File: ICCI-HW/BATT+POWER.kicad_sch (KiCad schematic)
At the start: 21 parts

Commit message: updated
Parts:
- removed D?: 3V3_LED, LED_SMD:LED_0603_1608Metric, symbol Device:LED
- removed J?: BATT IN, Connector_Molex:Molex_Micro-Fit_3.0_43650-0200_1x02_P3.00mm_Horizontal, symbol Connector_Generic:Conn_01x02
- removed R?: 510, Resistor_SMD:R_0603_1608Metric, symbol Device:R
- added BT? (x2): Li-Ion 18650, symbol Device:Battery_Cell
- added C? (x3): 10u, symbol Device:C
- added C?: 47u, symbol Device:C
- added D?: 1V8_LED, LED_SMD:LED_0603_1608Metric, symbol Device:LED
- added D?: 3V3_LED, LED_SMD:LED_0603_1608Metric, symbol Device:LED
- added D?: D_Schottky, symbol Device:D_Schottky
- added D?: TVS XXXXX, Diode_SMD:D_SMA, symbol Diode:1.5KExxA
- added JP?: SolderJumper_2_Open, symbol Jumper:SolderJumper_2_Open
- added Q? (x3): SSM3K15AMFV,L3F, symbol Device:Q_NMOS_GSD
- added R? (x3): R, symbol Device:R
- added R?: 680R, Resistor_SMD:R_0603_1608Metric, symbol Device:R
- added R?: 180R, Resistor_SMD:R_0603_1608Metric, symbol Device:R
- added U?: MAX77962EWJ12+, symbol ICCI-LIB:MAX77962EWJ12+
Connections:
- net +1V8: now also D?.2 (A)
- net +3V3: now also D?.2 (A), JP?.2 (B); no longer C?.1, C?.1, L?.2
- net GND: now also BT?.2 (-), C?.2, C?.2, C?.2, C?.2, D?.2 (A2), Q?.3 (D), Q?.3 (D), Q?.3 (D), R?.2, R?.2, U?.C5 (GND_1), U?.C6 (GND_2), U?.C7 (GND_3), U?.D1 (PGND_1), U?.D2 (PGND_2), U?.D3 (PGND_3), U?.D4 (PGND_4), U?.D6 (GND_4)
- net BATT_IN renamed SYS
- net SYS: now also C?.1, D?.1 (K), U?.E4 (SYS_1), U?.F1 (SYS_2), U?.F2 (SYS_3), U?.F3 (SYS_4), U?.F4 (SYS_5)
- net VCC renamed SW_VIN
- new net: C?.1, C?.1, JP?.1 (A), L?.2
- new net: Q?.2 (S), R?.2 (x2)
- new net: D?.1 (K), R?.1 (x2)
- new net: Q?.2 (S), R?.1
- new net: BT?.1 (+), BT?.2 (-)
- new net AVL: U?.A5 (AVL)
- new net BATT: BT?.1 (+), C?.1, D?.2 (A), U?.E5 (BATT_1), U?.F5 (BATT_2), U?.G5 (BATT_3)
- new net CHR0: Q?.1 (G)
- new net CHR1: Q?.1 (G)
- new net CHREN: Q?.1 (G)
- new net ISET: R?.1, R?.1, R?.2
- new net VBUS: C?.1, C?.1, D?.1 (A1), U?.B1 (CHGIN_1), U?.B2 (CHGIN_2), U?.B3 (CHGIN_3), U?.B4 (CHGIN_4)
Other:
- note added: "Analog GND"
- note added: "Buck test"
- note added: "Power GND"
- note added: "V_{OUT}=0.768(1+R_{1}/R_{2})"
- note removed: "L1 : Montare dopo aver testato che switching funziona"
- note removed: "V_{OUT}=0.768(1+R_{1}/R_{2}) For a V_{OUT}=3.3V the ratio should be 3.296875"
- moved on the sheet: C?, D?, F?, L?, R?, U?

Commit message: updated
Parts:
- removed JP?: SolderJumper_2_Open, symbol Jumper:SolderJumper_2_Open
- added R?: 0R, symbol Device:R
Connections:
- net +3V3: now also R?.2
- net at C?.1, C?.1, L?.2: now also R?.1
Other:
- moved on the sheet: BT?, C?, D?, F?, L?, Q?, R?, U?

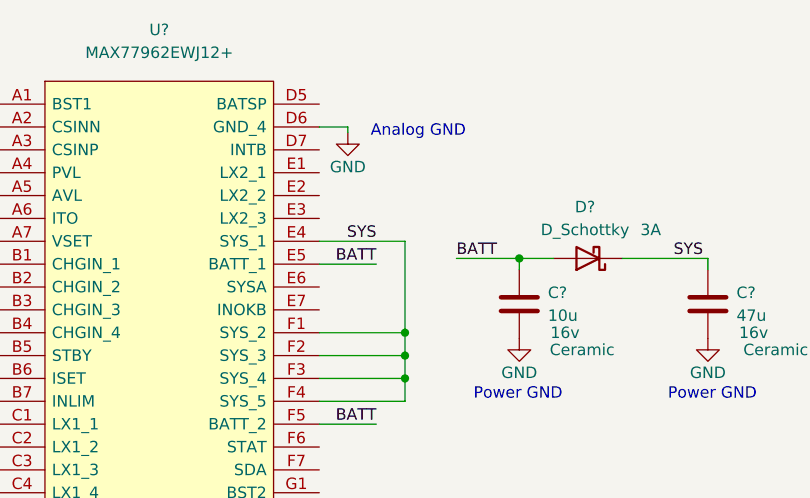
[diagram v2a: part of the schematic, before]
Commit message: add GPIO Expansion
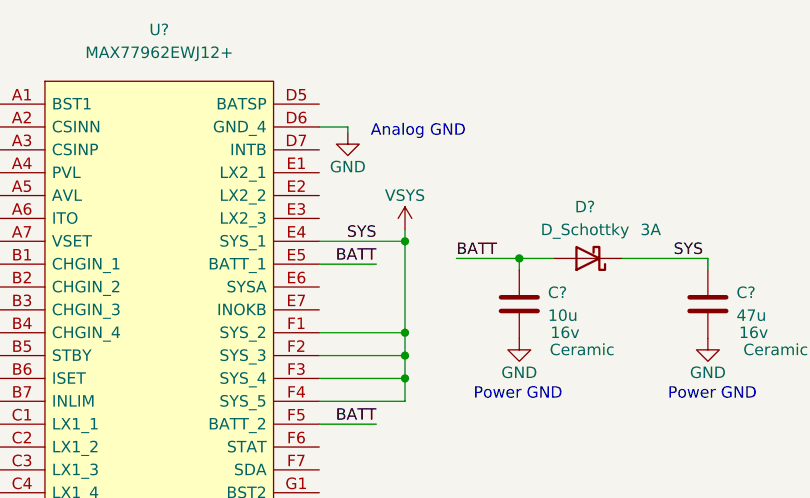
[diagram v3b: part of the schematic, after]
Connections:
- net SYS renamed VCC
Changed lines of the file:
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@@
   (junction (at 153.67 133.35) (diameter 0) (color 0 0 0 0)
   )
+  (junction (at 160.655 42.545) (diameter 0) (color 0 0 0 0)
+  )
   (junction (at 114.3 75.565) (diameter 0) (color 0 0 0 0)
   )
@@
   )
   (wire (pts (xy 160.655 52.705) (xy 160.655 55.245))
+    (stroke (width 0) (type default) (color 0 0 0 0))
+  )
+  (wire (pts (xy 160.655 41.275) (xy 160.655 42.545))
     (stroke (width 0) (type default) (color 0 0 0 0))
   )
@@
     (pin "2")
   )
+  (symbol (lib_id "power:VSYS") (at 160.655 41.275 0) (unit 1)
+    (in_bom yes) (on_board yes)
+    (property "Reference" "#PWR?" (id 0) (at 160.655 45.085 0)
+      (effects (font (size 1.27 1.27)) hide)
+    )
+    (property "Value" "VSYS" (id 1) (at 160.655 37.465 0))
+    (property "Footprint" "" (id 2) (at 160.655 41.275 0)
+      (effects (font (size 1.27 1.27)) hide)
+    )
+    (property "Datasheet" "" (id 3) (at 160.655 41.275 0)
+      (effects (font (size 1.27 1.27)) hide)
+    )
+    (pin "1")
+  )
   (symbol (lib_id "power:GND") (at 31.115 64.135 0) (unit 1)

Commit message: updated
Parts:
- removed C? (x3): 10u, symbol Device:C
- removed C?: 47u, symbol Device:C
- removed D?: TVS XXXXX, Diode_SMD:D_SMA, symbol Diode:1.5KExxA
- removed Q? (x3): SSM3K15AMFV,L3F, symbol Device:Q_NMOS_GSD
- removed R? (x3): R, symbol Device:R
- removed U?: MAX77962EWJ12+, symbol ICCI-LIB:MAX77962EWJ12+
- added C? (x2): 0.22u, symbol Device:C
- added C? (x3): 10u, symbol Device:C
- added C? (x2): 15n, symbol Device:C
- added C? (x2): 47u, symbol Device:C
- added C? (x2): 4.7u, symbol Device:C
- added C?: 100n, symbol Device:C
- added C?: 1u, Capacitor_SMD:C_0603_1608Metric, symbol Device:C
- added D?: 3V3_LED, LED_SMD:LED_0603_1608Metric, symbol Device:LED
- added JP? (x4): SolderJumper_3_Bridged12, symbol Jumper:SolderJumper_3_Bridged12
- added L?: 1.5u, symbol Device:L
- added NT?: NetTie_2, symbol Device:NetTie_2
- added R?: 680R, Resistor_SMD:R_0603_1608Metric, symbol Device:R
- added R?: 10m 1206 (?), symbol Device:R
- added R? (x2): 10k, symbol Device:R
- added R? (x2): 10R, symbol Device:R
- added R?: 4.7R, symbol Device:R
- added R?: 39,2k, symbol Device:R
- added R? (x2): 200k, symbol Device:R
- added R?: 140k, symbol Device:R
- added R?: 69,8k, symbol Device:R
- added R?: DNP, symbol Device:R
- added R?: 100k, symbol Device:R
- added RN?: 10k, Resistor_THT:R_Array_SIP4, symbol Device:R_Network03
- added TH?: NTC, symbol Device:Thermistor_NTC
- added U?: MAX77962EWJ12+, symbol ICCI-LIB:MAX77962EWJ12+
- D? (x2): Color Red -> Green
- D?: value SMA S1B -> RB160QS-40T18R
- F?: value 2016L050MR -> MF-LSMF075X
- R?: value 0R -> 0R BUCK TEST
- U?: value NCV8164ASN180T1G_ -> NCV8164ASN180T1G
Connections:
- net +3V3: now also D?.2 (A), R?.1
- net 1V8_EN: now also R?.2
- net AVL: now also C?.1, R?.1, R?.2, U?.A5 (AVL)
- net GND: now also C?.1, C?.1, C?.2, C?.2, C?.2, C?.2, C?.2, C?.2, C?.2, C?.2, R?.2, R?.2, R?.2, R?.2, RN?.1 (common), TH?.2, U?.C5 (GND_1), U?.C6 (GND_2), U?.C7 (GND_3), U?.D1 (PGND_1), U?.D2 (PGND_2), U?.D3 (PGND_3), U?.D4 (PGND_4), U?.D6 (GND_4), U?.G4 (BATSN)
- net ISET: now also JP?.2 (C), U?.B6 (ISET)
- net SCL1: now also U?.G7 (SCL)
- net SDA1: now also U?.F7 (SDA)
- net VBUS: now also R?.1, R?.1
- net VCC: now also C?.1, C?.1, U?.E4 (SYS_1), U?.F1 (SYS_2), U?.F2 (SYS_3), U?.F3 (SYS_4), U?.F4 (SYS_5)
- net 1V8_PG: no longer names the net of R?.2, U?.4 (PG)
- net BATT renamed +BATT
- net +BATT: now also C?.1, NT?.2, U?.E5 (BATT_1), U?.F5 (BATT_2), U?.G5 (BATT_3)
- new net: D?.1 (K), R?.1
- new net: C?.1, U?.G1 (BST2)
- new net: C?.2, L?.2, U?.E1 (LX2_1), U?.E2 (LX2_2), U?.E3 (LX2_3)
- new net: C?.1, U?.A1 (BST1)
- new net: C?.2, L?.1, U?.C1 (LX1_1), U?.C2 (LX1_2), U?.C3 (LX1_3), U?.C4 (LX1_4)
- new net BATSP: NT?.1, U?.D5 (BATSP)
- new net CHGIN: C?.1, C?.1, R?.1, R?.2, U?.B1 (CHGIN_1), U?.B2 (CHGIN_2), U?.B3 (CHGIN_3), U?.B4 (CHGIN_4)
- new net CSINN: C?.2, C?.2, R?.2, U?.A2 (CSINN)
- new net CSINP: C?.1, C?.2, R?.2, U?.A3 (CSINP)
- new net DISQBAT: RN?.3 (R2), U?.G2 (DISQBAT)
- new net INLIM: JP?.2 (C), U?.B7 (INLIM)
- new net INLIM_R: JP?.1 (A), R?.1
- new net ISET_R: JP?.3 (B), R?.1
- new net ITO: JP?.2 (C), U?.A6 (ITO)
- new net ITO_R: JP?.1 (A), R?.1
- new net MAX_INOKB: R?.2, U?.E7 (INOKB)
- new net MAX_INTB: R?.2, U?.D7 (INTB)
- new net OTGEN: RN?.2 (R1), U?.G3 (OTGEN)
- new net PVL: C?.1, JP?.1 (A), JP?.3 (B), JP?.3 (B), JP?.3 (B), R?.1, R?.1, R?.1, R?.1, U?.A4 (PVL)
- new net STAT: R?.2, U?.F6 (STAT)
- new net STBY: RN?.4 (R3), U?.B5 (STBY)
- new net SYSA: C?.1, U?.E6 (SYSA)
- new net THM: R?.2, TH?.1, U?.G6 (THM)
- new net VSET: JP?.2 (C), U?.A7 (VSET)
- new net VSET_R: JP?.1 (A), R?.1
- new net ~{BATT_S_LED}: R?.2
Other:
- note added: "0.75A Hold 1.5A Trip"
- note added: "1.5A"
- note added: "2A CHGIN"
- note added: "2S1P 18650 Li-Ion."
- note added: "3V3 Peripherals MAX absolute ratings: - ESP32 = 500mA (min required by DS) - GPIO Expander = 300mA (with all pin max output) - CP2102N = 50mA - 4 Sensors = 10mA - GPS/RTC = 70mA/50mA - Buzzer = 35mA -------------------------- TOT < 1.5A -> Real probably < 0.7A"
- note added: "75mA top-off"
- note added: "8.4V"
- note added: "==>"
- note added: "ATT!"
- note added: "As close as possible to battery terminals."
- note added: "Batt. Insertion Protection"
- note added: "Battery"
- note added: "Battery Management"
- note added: "Battery Status LED"
- note added: "Check if USB is max 1.5A. Sembrerebbe di no da USB BC 1.2"
- note added: "If at least one has no valid resistor value (ISET) charging is disabled by default and need to be set by I2C (choosen for safety reasons)."
- note added: "If batteries The regulator always priorities the system, the remaining power will be delivered to battery if charging. So, if charging at 1.5A and system is using 1A, battery charger will get only 0.5A. If Input power is not enough to power the system, battery will output current to system. So, if available input power is 0.5A and system is using 1A, if battery are charged they will deliver the r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"
- note added: "Led off batt normal, Led on batt charging, Led blinking slow batt low (in order to save energy)."
- note added: "Max 1.5A"
- note added: "NON DISPONIBILE"
- note added: "Tcold = 4.1 °C Thot = 53.2 °C"
- note added: "Temp Protection"
- note added: "WARNING, NO REVERSE POLARITY PROTECTION!"
- note removed: "1A"
- note removed: "2S1P 18650 Li-Ion"
- note removed: "Buck test"
- note removed: "Max XXA"
- note removed: "XXA Hold XXA Trip"
- moved on the sheet: BT?, C?, D?, F?, L?, R?, U?

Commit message: schematic V1.0
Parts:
- removed C?: 100n, Capacitor_SMD:C_0603_1608Metric, symbol Device:C
- removed C?: 10u, Capacitor_SMD:C_0805_2012Metric, symbol Device:C
- removed D?: 1V8_LED, LED_SMD:LED_0603_1608Metric, symbol Device:LED
- removed R?: 10k, Resistor_SMD:R_0603_1608Metric, symbol Device:R
- removed R?: 180R, Resistor_SMD:R_0603_1608Metric, symbol Device:R
- removed U?: TPS563201, Package_TO_SOT_SMD:SOT-23-6, symbol Regulator_Switching:TPS563200
- added U602: AP62301WU-7, symbol ICCI-LIB:AP62301WU-7
- C602: renamed from C?; Tech (none) -> Cer. low ESR; Voltage 16V -> 25V
- D603: renamed from D?; value RB160QS-40T18R -> PMEG3020EJ,115
- D605: renamed from D?; Color Green -> Red
- D606: renamed from D?; value D_Schottky -> VSSAF3L45HM3_A/I
- L601: renamed from L?; value 2.2u -> 3.3u
- R602, R615: renamed from R?; value 680R -> 510R
- R606: renamed from R?; value 33k -> 31,6k
- R607: renamed from R?; Tolerance (none) -> 1%
- R608: renamed from R?; value 10m 1206 (?) -> 10m; footprint (none) -> Resistor_SMD:R_1206_3216Metric; Package (none) -> 1206
- R619: renamed from R?; value 39,2k -> 22,6k
- gave numbers to parts that had none: 46
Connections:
- net +3V3: no longer R606.1
- net GND: now also U602.3 (GND)
- net SW_BST: now also U602.4 (BST)
- net SW_FB: now also U602.6 (FB)
- net SW_NODE: now also U602.2 (SW)
- net SW_VIN: now also U602.1 (VIN)
- net SW_NODE_OUT: now reaches C610.1, C612.1, L601.2, R614.1
- net SW_NODE_OUT: now also R606.1
- no-connect marks 0 -> 1
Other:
- note added: "2.5A Input max"
- note added: "2A"
- note added: "Check if USB BC is max 1.5A. From USB BC 1.2 Specs seems that I>1.5A are allowed."
- note added: "Floating for automatic startup"
- note added: "Low ESR"
- note removed: "1.5A"
- note removed: "2A CHGIN"
- note removed: "Check if USB is max 1.5A. Sembrerebbe di no da USB BC 1.2"
- note removed: "NON DISPONIBILE"
- note removed: "V_{OUT}=0.768(1+R_{1}/R_{2})"
- moved on the sheet: C602, C608, C610, C612, D602, D603, D605, F601, L601, R606, R607, R614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

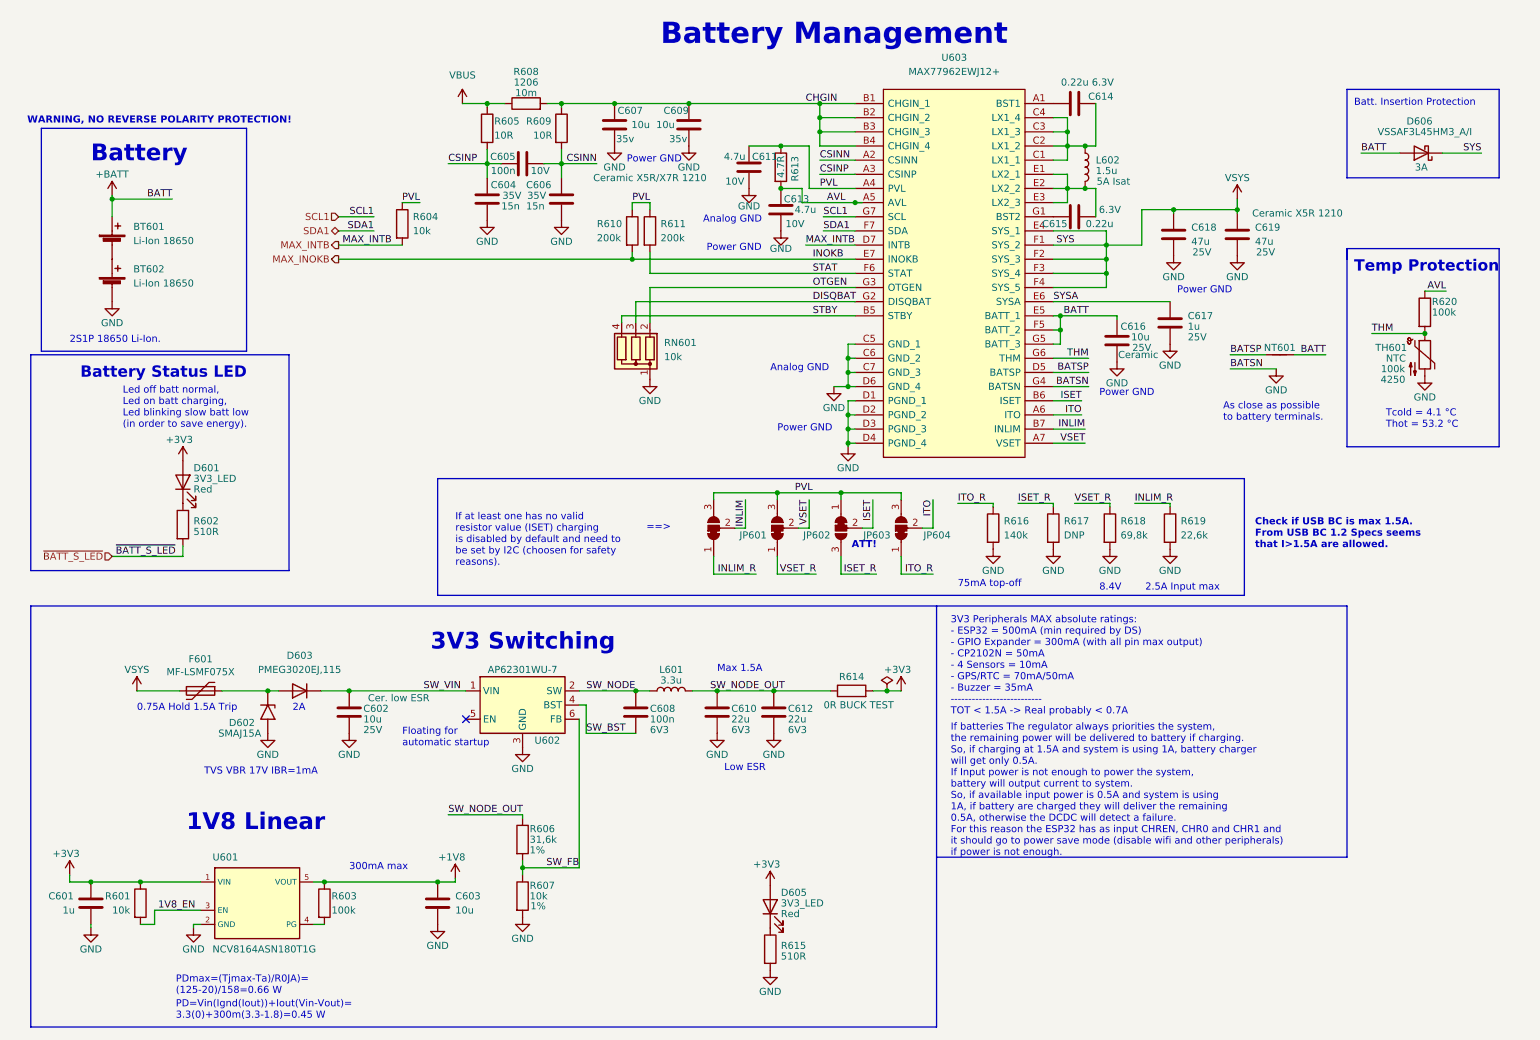
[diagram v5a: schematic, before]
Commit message: footprint assigned
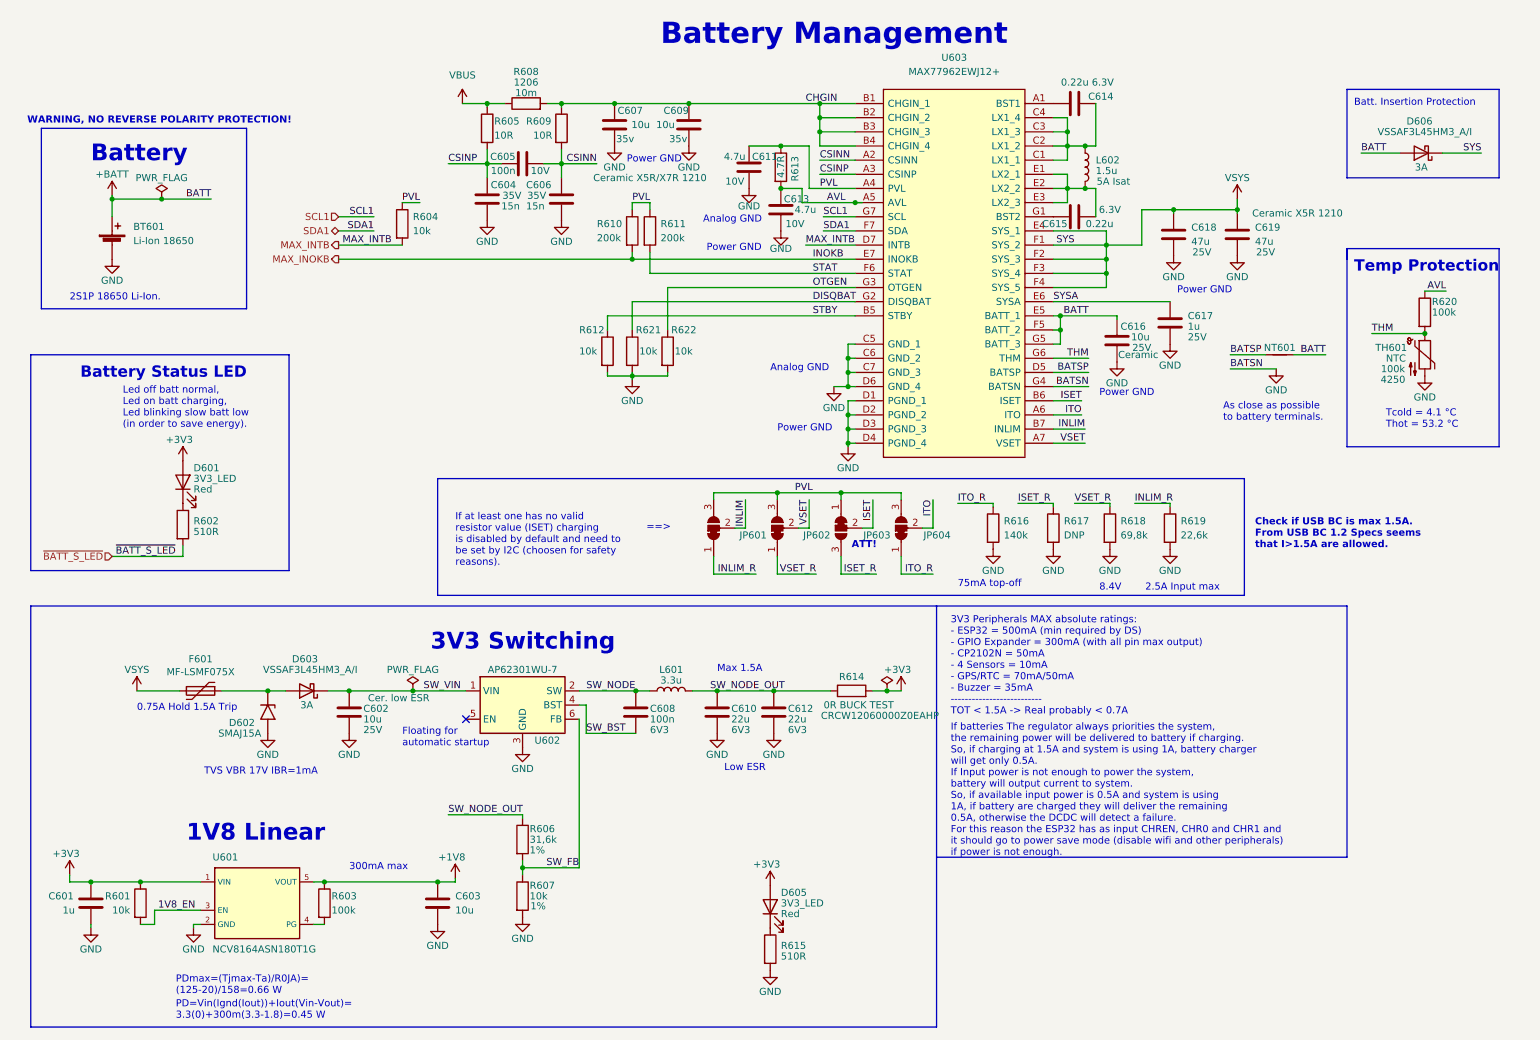
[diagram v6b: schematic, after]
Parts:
- removed BT602: Li-Ion 18650, symbol Device:Battery_Cell
- removed D603: PMEG3020EJ,115, Diode_SMD:D_SMA, symbol Diode:1N4007
- removed RN601: 10k, Resistor_THT:R_Array_SIP4, symbol Device:R_Network03
- added D603: VSSAF3L45HM3_A/I, ICCI-LIB:VSSAF3L45HM3, symbol Device:D_Schottky
- added R612, R621, R622: 10k, Resistor_SMD:R_0603_1608Metric, symbol Device:R
- BT601: footprint (none) -> ICCI-LIB:BAT_1048
- C601, C604, C605, C606, C611, C613, C614, C615: footprint (none) -> Capacitor_SMD:C_0603_1608Metric
- C603, C607, C609, C616: footprint (none) -> Capacitor_SMD:C_0805_2012Metric
- C610, C612: footprint Capacitor_SMD:C_0805_2012Metric -> Capacitor_SMD:C_1206_3216Metric
- C618, C619: footprint (none) -> Capacitor_SMD:C_1210_3225Metric
- D601, D605: footprint LED_SMD:LED_0603_1608Metric -> LED_SMD:LED_0805_2012Metric
- D602: footprint Diode_SMD:D_SMA -> ICCI-LIB:SMAJ15A
- D606: footprint (none) -> ICCI-LIB:VSSAF3L45HM3
- F601: footprint ppse_2021:2016L Series PPTC -> ICCI-LIB:Bourns_MF-LSMF
- JP601, JP602, JP603, JP604: footprint (none) -> Jumper:SolderJumper-3_P1.3mm_Open_RoundedPad1.0x1.5mm_NumberLabels
- L601: footprint ppse_2021:Inductor -> Inductor_SMD:L_Bourns_SRP7028A_7.3x6.6mm; Model (none) -> SRP7020TA-3R3M
- L602: footprint (none) -> Inductor_SMD:L_Coilcraft_XxL4040
- NT601: footprint (none) -> NetTie:NetTie-2_SMD_Pad2.0mm
- R601, R603, R604, R605, R609, R610, R611, R613, R616, R617, R618, R619, R620: footprint (none) -> Resistor_SMD:R_0603_1608Metric
- R614: footprint (none) -> Resistor_SMD:R_1206_3216Metric; Model (none) -> CRCW12060000Z0EAHP
- TH601: footprint (none) -> Resistor_SMD:R_0603_1608Metric; Model ABNTC-0402-104J-4250F-T -> ABNTC-0603-104J-4250F-T
- U601: footprint (none) -> ICCI-LIB:NCV8164ASN180T1G
- U602: footprint (none) -> Package_TO_SOT_SMD:TSOT-23-6
- U603: footprint (none) -> ICCI-LIB:MAX77962EWJ12+
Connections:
- net DISQBAT: now also R621.1
- net GND: now also BT601.2 (-), R612.2, R621.2, R622.2
- net OTGEN: now also R622.1
- net STBY: now also R612.1
- net SW_VIN: now also D603.1 (K)
- net at D602.1 (A1), F601.1: now also D603.2 (A)
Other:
- note removed: "2A"
